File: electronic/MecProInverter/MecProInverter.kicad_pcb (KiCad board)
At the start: 4 copper layers, 104 x 168 mm, 169 parts, among them J10 Net, J3 ISO_Data, J4 Motor, J5 Display, J6 MAX312820, J7 Test, J8 U_ZK, J9 U_VS, K2 RT314A12, Q1 DMN3404L, Q2 DMN3404L, SW1 PTS645SM95SMTR92LFS, SW2 PTS645SM95SMTR92LFS, SW3 PTS645SM95SMTR92LFS, U1 ESP32-S3-MINI-1-N8, U10 CC6904SO-30A, U11 CC6904SO-30A, U12 TEA1-0505HI, U13 IKCM20L60GA, U14 PSRV05-4MR6T1G, U15 ADUM1201ARZ-RL7, U16 ADUM1201ARZ-RL7, U17 PSRV05-4MR6T1G, U18 PMV100EPAR, U19 PSRV05-4MR6T1G, U2 ADUM3160, U20 PSRV05-4MR6T1G, U21 RK09D113000F_10k, U3 TYPE-C_16PIN_2MD(073), U4 LVE2560E, U5 TPS563201DDCR, U6 SKRKAEE020, U7 SKRKAEE020, U8 TLA2528IRTER, U9 CC6904SO-30A

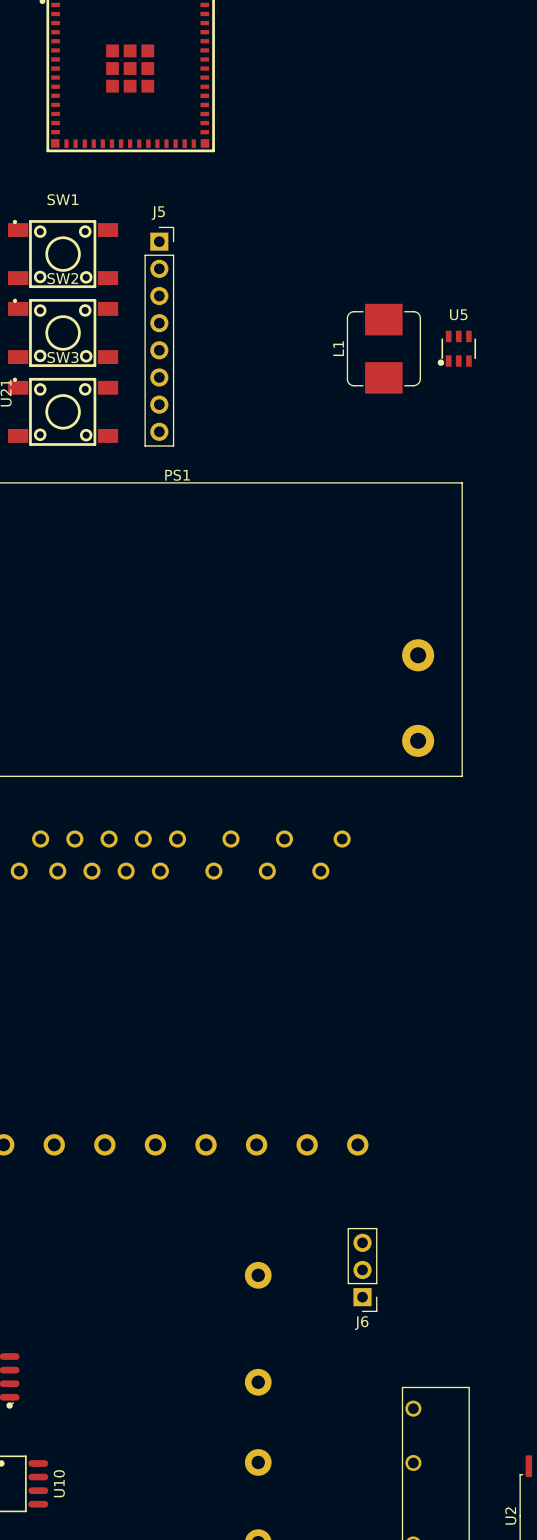
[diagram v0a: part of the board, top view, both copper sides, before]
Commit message: Electronic
Added 3d Moodel on Layout
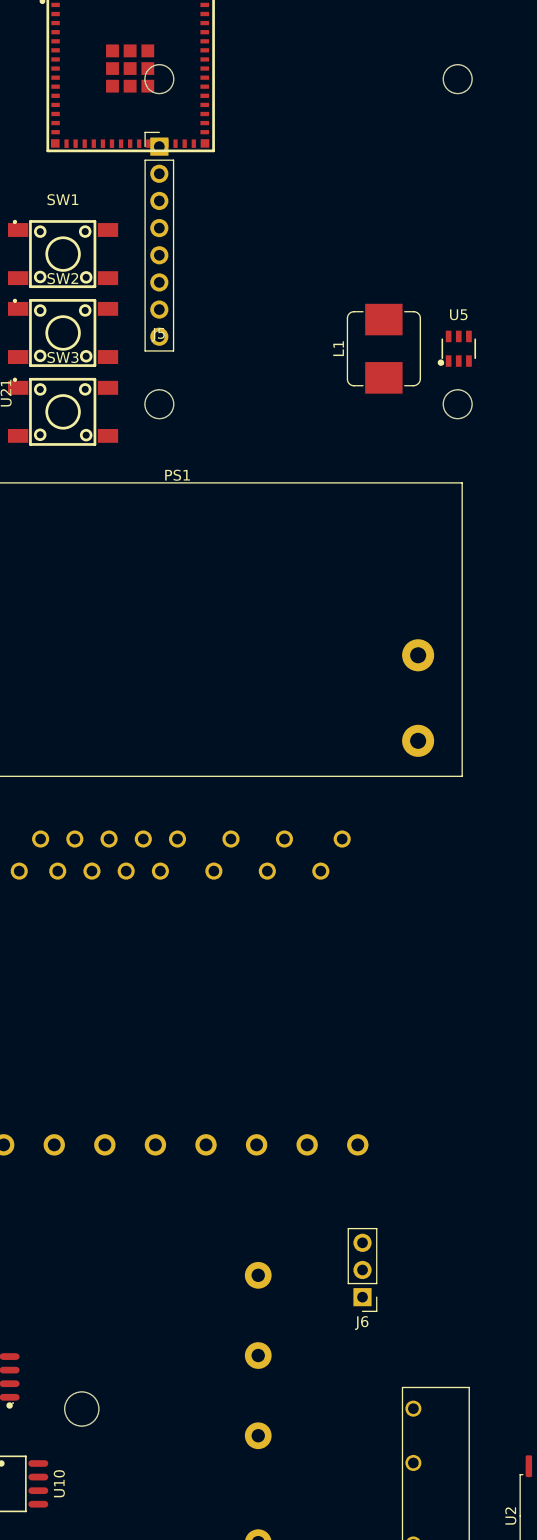
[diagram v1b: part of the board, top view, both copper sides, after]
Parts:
- J5: footprint Connector_PinSocket_2.54mm:PinSocket_1x08_P2.54mm_Vertical -> Own_Footprint:Adafruit_938
- U4: footprint Own_Library:LVE2560E -> Own_Footprint:LVE2560E
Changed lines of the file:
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@@
     )
   )
-  (footprint "Connector_PinSocket_2.54mm:PinSocket_1x08_P2.54mm_Vertical" (layer "F.Cu")
+  (footprint "Own_Footprint:Adafruit_938" (layer "F.Cu")
     (at 131 82.84)
-    (descr "Through hole straight socket strip, 1x08, 2.54mm pitch, single row (from Kicad 4.0.7), script generated")
-    (tags "Through hole socket strip THT 1x08 2.54mm single row")
     (property "Sheetfile" "control.kicad_sch")
     (property "Sheetname" "Control")
@@
     (property "ki_keywords" "connector")
     (attr through_hole)
-    (fp_text reference "J5" (at 0 -2.77) (layer "F.SilkS")
+    (fp_text reference "J5" (at 0 8.61 unlocked) (layer "F.SilkS")
+        (effects (font (size 1 1) (thickness 0.1)))
+    )
+    (fp_text value "Display" (at 0 10.11 unlocked) (layer "F.Fab")
         (effects (font (size 1 1) (thickness 0.15)))
     )
-    (fp_text value "Display" (at 0 20.55) (layer "F.Fab")
+    (fp_text user "${REFERENCE}" (at 0 0 90) (layer "F.Fab")
         (effects (font (size 1 1) (thickness 0.15)))
     )
-    (fp_text user "${REFERENCE}" (at 0 8.89 90) (layer "F.Fab")
+    (fp_text user "${REFERENCE}" (at 0 11.36 unlocked) (layer "F.Fab")
         (effects (font (size 1 1) (thickness 0.15)))
     )
-    (fp_line (start -1.33 1.27) (end -1.33 19.11)
+    (fp_line (start -1.33 -10.22) (end 0 -10.22)
       (stroke (width 0.12) (type solid)) (layer "F.SilkS"))
-    (fp_line (start -1.33 1.27) (end 1.33 1.27)
+    (fp_line (start -1.33 -8.89) (end -1.33 -10.22)
       (stroke (width 0.12) (type solid)) (layer "F.SilkS"))
-    (fp_line (start -1.33 19.11) (end 1.33 19.11)
+    (fp_line (start -1.33 -7.62) (end -1.33 10.22)
       (stroke (width 0.12) (type solid)) (layer "F.SilkS"))
-    (fp_line (start 0 -1.33) (end 1.33 -1.33)
+    (fp_line (start -1.33 -7.62) (end 1.33 -7.62)
       (stroke (width 0.12) (type solid)) (layer "F.SilkS"))
-    (fp_line (start 1.33 -1.33) (end 1.33 0)
+    (fp_line (start -1.33 10.22) (end 1.33 10.22)
       (stroke (width 0.12) (type solid)) (layer "F.SilkS"))
-    (fp_line (start 1.33 1.27) (end 1.33 19.11)
+    (fp_line (start 1.33 -7.62) (end 1.33 10.22)
       (stroke (width 0.12) (type solid)) (layer "F.SilkS"))
-    (fp_line (start -1.8 -1.8) (end 1.75 -1.8)
+    (fp_circle (center 0 -15.2) (end 1.35 -15.2)
+      (stroke (width 0.1) (type default)) (fill none) (layer "Edge.Cuts"))
+    (fp_circle (center 0 15.2) (end 1.35 15.2)
+      (stroke (width 0.1) (type default)) (fill none) (layer "Edge.Cuts"))
+    (fp_circle (center 27.9 -15.2) (end 29.25 -15.2)
+      (stroke (width 0.1) (type default)) (fill none) (layer "Edge.Cuts"))
+    (fp_circle (center 27.9 15.2) (end 29.25 15.2)
+      (stroke (width 0.1) (type default)) (fill none) (layer "Edge.Cuts"))
+    (fp_line (start -1.8 -10.69) (end -1.8 10.66)
       (stroke (width 0.05) (type solid)) (layer "F.CrtYd"))
-    (fp_line (start -1.8 19.55) (end -1.8 -1.8)
+    (fp_line (start -1.8 10.66) (end 1.8 10.66)
       (stroke (width 0.05) (type solid)) (layer "F.CrtYd"))
-    (fp_line (start 1.75 -1.8) (end 1.75 19.55)
+    (fp_line (start 1.8 -10.69) (end -1.8 -10.69)
       (stroke (width 0.05) (type solid)) (layer "F.CrtYd"))
-    (fp_line (start 1.75 19.55) (end -1.8 19.55)
+    (fp_line (start 1.8 10.66) (end 1.8 -10.69)
       (stroke (width 0.05) (type solid)) (layer "F.CrtYd"))
-    (fp_line (start -1.27 -1.27) (end 0.635 -1.27)
+    (fp_line (start -1.27 -9.525) (end -0.635 -10.16)
       (stroke (width 0.1) (type solid)) (layer "F.Fab"))
-    (fp_line (start -1.27 19.05) (end -1.27 -1.27)
+    (fp_line (start -1.27 10.16) (end -1.27 -9.525)
       (stroke (width 0.1) (type solid)) (layer "F.Fab"))
-    (fp_line (start 0.635 -1.27) (end 1.27 -0.635)
+    (fp_line (start -0.635 -10.16) (end 1.27 -10.16)
       (stroke (width 0.1) (type solid)) (layer "F.Fab"))
-    (fp_line (start 1.27 -0.635) (end 1.27 19.05)
+    (fp_line (start 1.27 -10.16) (end 1.27 10.16)
       (stroke (width 0.1) (type solid)) (layer "F.Fab"))
-    (fp_line (start 1.27 19.05) (end -1.27 19.05)
+    (fp_line (start 1.27 10.16) (end -1.27 10.16)
       (stroke (width 0.1) (type solid)) (layer "F.Fab"))
-    (pad "1" thru_hole rect (at 0 0) (size 1.7 1.7) (drill 1) (layers "*.Cu" "*.Mask")
+    (pad "1" thru_hole rect (at 0 -8.89) (size 1.7 1.7) (drill 1) (layers "*.Cu" "*.Mask")
       (net 112 "Net-(J5-Pin_1)") (pinfunction "Pin_1") (pintype "passive"))
-    (pad "2" thru_hole oval (at 0 2.54) (size 1.7 1.7) (drill 1) (layers "*.Cu" "*.Mask")
+    (pad "2" thru_hole oval (at 0 -6.35) (size 1.7 1.7) (drill 1) (layers "*.Cu" "*.Mask")
       (net 113 "Net-(J5-Pin_2)") (pinfunction "Pin_2") (pintype "passive"))
-    (pad "3" thru_hole oval (at 0 5.08) (size 1.7 1.7) (drill 1) (layers "*.Cu" "*.Mask")
+    (pad "3" thru_hole oval (at 0 -3.81) (size 1.7 1.7) (drill 1) (layers "*.Cu" "*.Mask")
       (net 115 "Net-(J5-Pin_3)") (pinfunction "Pin_3") (pintype "passive"))
-    (pad "4" thru_hole oval (at 0 7.62) (size 1.7 1.7) (drill 1) (layers "*.Cu" "*.Mask")
+    (pad "4" thru_hole oval (at 0 -1.27) (size 1.7 1.7) (drill 1) (layers "*.Cu" "*.Mask")
       (net 116 "Net-(J5-Pin_4)") (pinfunction "Pin_4") (pintype "passive"))
-    (pad "5" thru_hole oval (at 0 10.16) (size 1.7 1.7) (drill 1) (layers "*.Cu" "*.Mask")
+    (pad "5" thru_hole oval (at 0 1.27) (size 1.7 1.7) (drill 1) (layers "*.Cu" "*.Mask")
       (net 117 "Net-(J5-Pin_5)") (pinfunction "Pin_5") (pintype "passive"))
-    (pad "6" thru_hole oval (at 0 12.7) (size 1.7 1.7) (drill 1) (layers "*.Cu" "*.Mask")
+    (pad "6" thru_hole oval (at 0 3.81) (size 1.7 1.7) (drill 1) (layers "*.Cu" "*.Mask")
       (net 122 "Net-(J5-Pin_6)") (pinfunction "Pin_6") (pintype "passive"))
-    (pad "7" thru_hole oval (at 0 15.24) (size 1.7 1.7) (drill 1) (layers "*.Cu" "*.Mask")
+    (pad "7" thru_hole oval (at 0 6.35) (size 1.7 1.7) (drill 1) (layers "*.Cu" "*.Mask")
       (net 3 "+3.3V") (pinfunction "Pin_7") (pintype "passive"))
-    (pad "8" thru_hole oval (at 0 17.78) (size 1.7 1.7) (drill 1) (layers "*.Cu" "*.Mask")
+    (pad "8" thru_hole oval (at 0 8.89) (size 1.7 1.7) (drill 1) (layers "*.Cu" "*.Mask")
       (net 2 "GND") (pinfunction "Pin_8") (pintype "passive"))
-    (model "${KICAD6_3DMODEL_DIR}/Connector_PinSocket_2.54mm.3dshapes/PinSocket_1x08_P2.54mm_Vertical.wrl"
-      (offset (xyz 0 0 0))
+    (model "C:/GitHub/MecProInverter/electronic/own_library/footprint/packages3d/938 Mono 128x64 OLED Stemma.step"
+      (offset (xyz 30.48 17.78 16.5))
       (scale (xyz 1 1 1))
-      (rotate (xyz 0 0 0))
+      (rotate (xyz 180 0 90))
     )
   )
@@
     )
   )
-  (footprint "Own_Library:LVE2560E" (layer "B.Cu")
+  (footprint "Own_Footprint:LVE2560E" (layer "B.Cu")
     (at 140.25 179.5 -90)
     (property "Sheetfile" "power.kicad_sch")
@@
     (property "ki_description" "LVE2560E")
     (attr through_hole)
-    (fp_text reference "U4" (at 12.5 8 -270 unlocked) (layer "B.SilkS")
+    (fp_text reference "U4" (at 12.5 8 90 unlocked) (layer "B.SilkS")
         (effects (font (size 1 1) (thickness 0.1)) (justify mirror))
     )
-    (fp_text value " LVE2560E" (at 12.5 6.5 -270 unlocked) (layer "B.Fab")
+    (fp_text value " LVE2560E" (at 12.5 6.5 90 unlocked) (layer "B.Fab")
         (effects (font (size 1 1) (thickness 0.15)) (justify mirror))
     )
-    (fp_text user "${REFERENCE}" (at 12.5 5 -270 unlocked) (layer "B.Fab")
+    (fp_text user "${REFERENCE}" (at 12.5 5 90 unlocked) (layer "B.Fab")
         (effects (font (size 1 1) (thickness 0.15)) (justify mirror))
     )
     (fp_rect (start -2.5 2.5) (end 27.5 -2.5)
       (stroke (width 0.1) (type default)) (fill none) (layer "B.SilkS"))
-    (fp_rect (start -2.5 25) (end 27.5 -2.5)
+    (fp_rect (start -2.5 25.5) (end 27.5 -2.5)
       (stroke (width 0.1) (type default)) (fill none) (layer "B.SilkS"))
+    (fp_circle (center 12.5 16.5) (end 14.1 16.5)
+      (stroke (width 0.1) (type default)) (fill none) (layer "Edge.Cuts"))
     (pad "1" thru_hole circle (at 0 0 270) (size 2.5 2.5) (drill 1.25) (layers "*.Cu" "*.Mask")
       (net 152 "Net-(U4-VDD)") (pinfunction "VDD") (pintype "power_out"))
-    (pad "2" thru_hole circle (at 10 0 270) (size 2.5 2.5) (drill 1.25) (layers "*.Cu" "*.Mask")
+    (pad "2" thru_hole circle (at 7.5 0 270) (size 2.5 2.5) (drill 1.25) (layers "*.Cu" "*.Mask")
       (net 92 "Net-(U4-~Phase)") (pinfunction "~Phase") (pintype "power_in"))
-    (pad "3" thru_hole circle (at 17.5 0 270) (size 2.5 2.5) (drill 1.25) (layers "*.Cu" "*.Mask")
+    (pad "3" thru_hole circle (at 15 0 270) (size 2.5 2.5) (drill 1.25) (layers "*.Cu" "*.Mask")
       (net 114 "/Power/AC_N") (pinfunction "~Neutral") (pintype "power_in"))
     (pad "4" thru_hole circle (at 25 0 270) (size 2.5 2.5) (drill 1.25) (layers "*.Cu" "*.Mask")
       (net 2 "GND") (pinfunction "GND") (pintype "power_out"))
+    (model "C:/GitHub/MecProInverter/electronic/own_library/footprint/packages3d/BrueckenGR_LVE2560E.stp"
+      (offset (xyz 27.5 5.5 -1.5))
+      (scale (xyz 1 1 1))
+      (rotate (xyz 0 0 0))
+    )
   )
   (gr_rect locked (start 94 53) (end 198 221)

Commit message: Electronic
Schematic V1.0
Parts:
- removed C44: 0.1nF, Capacitor_SMD:C_0603_1608Metric
- added C14: 4.7uF, Capacitor_SMD:C_0603_1608Metric, F.Cu at (60.9, 113.2)
- added C15: 100nF, Capacitor_SMD:C_0603_1608Metric, F.Cu at (60.9, 115.7)
- added C16: 100nF, Capacitor_SMD:C_0603_1608Metric, F.Cu at (60.9, 118.2)
- added C17: 4.7uF, Capacitor_SMD:C_0603_1608Metric, F.Cu at (60.9, 120.7)
- added C18: 4.7uF, Capacitor_SMD:C_0603_1608Metric, F.Cu at (60.9, 123.2)
- added C19: 100nF, Capacitor_SMD:C_0603_1608Metric, F.Cu at (60.9, 125.7)
- added C53: 100nF, Capacitor_SMD:C_0603_1608Metric, F.Cu at (65.0, 113.2)
- added C54: 100nF, Capacitor_SMD:C_0603_1608Metric, F.Cu at (65.0, 115.7)
- added C55: 100nF, Capacitor_SMD:C_0603_1608Metric, F.Cu at (65.0, 118.2)
- added C56: 100nF, Capacitor_SMD:C_0603_1608Metric, F.Cu at (65.0, 120.7)
- added D10: D, Diode_SMD:D_0603_1608Metric, F.Cu at (69.0, 118.4)
- added D11: D, Diode_SMD:D_0603_1608Metric, F.Cu at (69.0, 121.0)
- added D8: D, Diode_SMD:D_0603_1608Metric, F.Cu at (69.0, 113.2)
- added D9: D, Diode_SMD:D_0603_1608Metric, F.Cu at (69.0, 115.8)
- added R1: 14.4, Own_Footprint:PWR220T-20, B.Cu at (103.5, 204.0)
- added R65: 10M, Resistor_SMD:R_0603_1608Metric, F.Cu at (65.0, 123.2)
- C10, C11, C12, C13, C20, C5, C6, C7, C8, C9: footprint Capacitor_SMD:C_0201_0603Metric -> Capacitor_SMD:C_0603_1608Metric
- C41, C42: value 0.1nF -> 100nF
- R10, R11, R12, R13, R14, R15, R16, R17, R19, R2, R20, R21, R22, R23, R24, R25, R26, R27, R28, R29, R3, R30, R4, R5, R6, R7, R8, R9: footprint Resistor_SMD:R_0201_0603Metric -> Resistor_SMD:R_0603_1608Metric
- R32, R33, R34, R36, R37, R38, R39, R40, R41, R42, R47, R48, R49, R50, R51, R52, R53, R54, R55, R56, R57, R58, R59, R61, R62: footprint Resistor_SMD:R_0201_0603Metric_Pad0.64x0.40mm_HandSolder -> Resistor_SMD:R_0603_1608Metric
- R35: value 999m -> 999M; footprint Resistor_SMD:R_0201_0603Metric_Pad0.64x0.40mm_HandSolder -> Resistor_SMD:R_0603_1608Metric
- R43, R44, R45: value 100 -> 10M; footprint Resistor_SMD:R_0201_0603Metric_Pad0.64x0.40mm_HandSolder -> Resistor_SMD:R_0603_1608Metric
- R60: value 999m -> 330; footprint Resistor_SMD:R_0201_0603Metric_Pad0.64x0.40mm_HandSolder -> Resistor_SMD:R_0603_1608Metric
- TP1, TP2, TP3, TP4, TP5, TP6, TP7, TP8: footprint TestPoint:TestPoint_Pad_D2.0mm -> TestPoint:TestPoint_Pad_D1.5mm
- moved U5 133.1 mm to (32.0, 53.1)
- moved L1 119.7 mm to (39.6, 51.8)
- moved D3 68.0 mm to (173.0, 65.0)
- moved PS1 50.4 mm to (154.8, 132.3), turned to 180 degrees
- moved J7 43.5 mm to (96.0, 111.7), turned to 180 degrees
- moved K2 27.3 mm to (99.2, 152.8), turned to -90 degrees
- moved U21 25.6 mm to (103.0, 71.6), turned to 180 degrees
- moved J10 21.5 mm to (107.0, 215.5)
- moved J4 21.5 mm to (128.5, 215.5)
- moved SW1 20.2 mm to (119.0, 64.0)
- moved U8 19.1 mm to (124.5, 184.3)
- moved U7 18.0 mm to (121.0, 56.0), turned to 0 degrees
- moved U1 17.7 mm to (146.0, 66.0)
- moved U10 17.1 mm to (133.0, 205.0)
- moved Q1 16.8 mm to (109.0, 146.0)
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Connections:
- C41 pad 2: /Power/CURRENT_AC -> Net-(D9-K)
- C42 pad 2: Net-(U8-AIN3/GPIO3) -> Net-(D10-K)
- K2 pad 11: /Power/AC_L -> Net-(U4-~Phase)
- K2 pad 14: Net-(U4-~Phase) -> /Power/AC_L
- R43 pad 1: Net-(U9-OUT) -> Net-(D9-K)
- R43 pad 2: /Power/CURRENT_AC -> GND
- R44 pad 1: Net-(U10-OUT) -> Net-(D10-K)
- R44 pad 2: Net-(U8-AIN3/GPIO3) -> GND
- R45 pad 1: Net-(U11-OUT) -> Net-(D11-K)
- R45 pad 2: Net-(U8-AIN4/GPIO4) -> GND
- R47 pad 1: Net-(U8-AIN2/GPIO2) -> Net-(D11-A)
- R60 pad 2: GND -> Net-(U13-ITRIP)
- R64 pad 2: Net-(U8-AIN2/GPIO2) -> Net-(D11-A)
- U10 pad 7: Net-(U10-OUT) -> Net-(D9-A)
- U11 pad 7: Net-(U11-OUT) -> Net-(D10-A)
- U8 pad 1: Net-(U8-AIN2/GPIO2) -> Net-(D11-K)
- U8 pad 2: Net-(U8-AIN3/GPIO3) -> Net-(D9-K)
- U8 pad 3: Net-(U8-AIN4/GPIO4) -> Net-(D10-K)
- U9 pad 7: Net-(U9-OUT) -> Net-(D8-A)
